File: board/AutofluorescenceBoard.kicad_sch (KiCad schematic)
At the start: 39 parts, among them Q1 Q_PMOS, U1 PAM2863ECR, U2 PAM2863ECR, U3 PAM2863ECR

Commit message: Added LED Footprints and started Layout
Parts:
- D1: footprint (none) -> AF Board:405nm LED
- D3: footprint (none) -> AF Board:365nm LED
- D5: footprint (none) -> AF Board:490nm LED
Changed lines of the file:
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@@
 			)
 		)
-		(property "Footprint" ""
+		(property "Footprint" "AF Board:365nm LED"
 			(at 129.54 31.75 0)
 			(effects
@@
 			)
 		)
-		(property "Footprint" ""
+		(property "Footprint" "AF Board:490nm LED"
 			(at 130.81 139.7 0)
 			(effects
@@
 			)
 		)
-		(property "Footprint" ""
+		(property "Footprint" "AF Board:405nm LED"
 			(at 129.54 87.63 0)
 			(effects

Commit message: Layout Start
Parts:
- D8: footprint ESDALC14-1BF4:ESDALC14-1BF4 -> Resistor_SMD:R_0603_1608Metric
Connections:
- net GND: no longer U2.8 (PGND)
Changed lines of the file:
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@@
 	)
 	(junction
-		(at 107.95 102.87)
-		(diameter 0)
-		(color 0 0 0 0)
-	)
-	(junction
 		(at 60.96 100.33)
 		(diameter 0)
@@
 	)
 	(junction
-		(at 107.95 95.25)
-		(diameter 0)
-		(color 0 0 0 0)
-	)
-	(junction
-		(at 107.95 92.71)
-		(diameter 0)
-		(color 0 0 0 0)
-	)
-	(junction
 		(at 41.91 41.91)
 		(diameter 0)
@@
 	(wire
 		(pts
-			(xy 107.95 92.71) (xy 107.95 95.25)
+			(xy 107.95 92.71) (xy 107.95 97.79)
 		)
 		(stroke
@@
 	(wire
 		(pts
-			(xy 107.95 95.25) (xy 107.95 97.79)
-		)
-		(stroke
-			(width 0)
-			(type default)
-		)
-	)
-	(wire
-		(pts
 			(xy 257.81 83.82) (xy 257.81 86.36)
 		)
@@
 			)
 		)
-		(property "Footprint" "ESDALC14-1BF4:ESDALC14-1BF4"
+		(property "Footprint" "Resistor_SMD:R_0603_1608Metric"
 			(at 256.54 31.75 0)
 			(effects

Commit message: Random Footprint changes
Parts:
- removed D2, D4, D6: D_Schottky, AF Board:Schottky, symbol Device:D_Schottky
- removed D8: D_TVS, Resistor_SMD:R_0603_1608Metric, symbol Device:D_TVS
- removed Q1: Q_PMOS, AF Board:P-MOSFET, symbol Device:Q_PMOS
- removed R5: 10K, AF Board:RES_R0603_ROM-L, symbol Device:R_US
- added CR1, CR2, CR3: SK34A-LTP, SMADO-214AC_MCC, symbol AutofluorescenceBoard:SK34A-LTP
- C1, C2, C3: footprint AF Board:CAP_CL_21_SAM-L -> Capacitor_SMD:C_0805_2012Metric_Pad1.18x1.45mm_HandSolder
- L1, L2, L3: footprint AF Board:Inductor -> AutofluorescenceBoard:SRN6045TA-470M
- R1, R2, R3: value 0.1R -> 0.1; footprint AF Board:TO508P1229X317-3N -> AutofluorescenceBoard:TO508P1229X317-3N
- R4: renamed from R6; footprint AF Board:RES_R0603_ROM-L -> Resistor_SMD:R_0603_1608Metric_Pad0.98x0.95mm_HandSolder
- R5: renamed from R7; footprint AF Board:RES_R0603_ROM-L -> Resistor_SMD:R_0603_1608Metric_Pad0.98x0.95mm_HandSolder
- R6: renamed from R8; footprint AF Board:RES_R0603_ROM-L -> Resistor_SMD:R_0603_1608Metric_Pad0.98x0.95mm_HandSolder
- R7: renamed from R4; footprint AF Board:2.2K Res -> Resistor_SMD:R_0603_1608Metric_Pad0.98x0.95mm_HandSolder
- U1, U2, U3: footprint AF Board:LED_IC -> SOIC_863ECR_DIO; symbol 2025-10-08_01-46-07:PAM2863ECR -> AutofluorescenceBoard:PAM2863ECR
- renumbered D3 to D1, D1 to D2, D5 to D3, D7 to D4
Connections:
- net +12V: now also Conn1.2 (V+Log), CR1.1, CR2.1, CR3.1
- net GND: now also R1.3, R2.3, R3.3; no longer R1.2, R2.2, R3.2
- net at F3.1, TP3.1, U3.2 (ISENSE): now also R3.2; no longer R3.3
- net at L3.2, U3.5 (LX), U3.6 (LX): now also CR3.2
- net at F2.1, TP2.1, U2.2 (ISENSE): now also R2.2; no longer R2.3
- net at L2.2, U2.5 (LX), U2.6 (LX): now also CR2.2
- net at F1.1, TP1.1, U1.2 (ISENSE): now also R1.2; no longer R1.3
- net at L1.2, U1.5 (LX), U1.6 (LX): now also CR1.2
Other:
- note added: "TODO: Reverse Polarity Protection"
- moved on the sheet: Conn1A, Conn1B

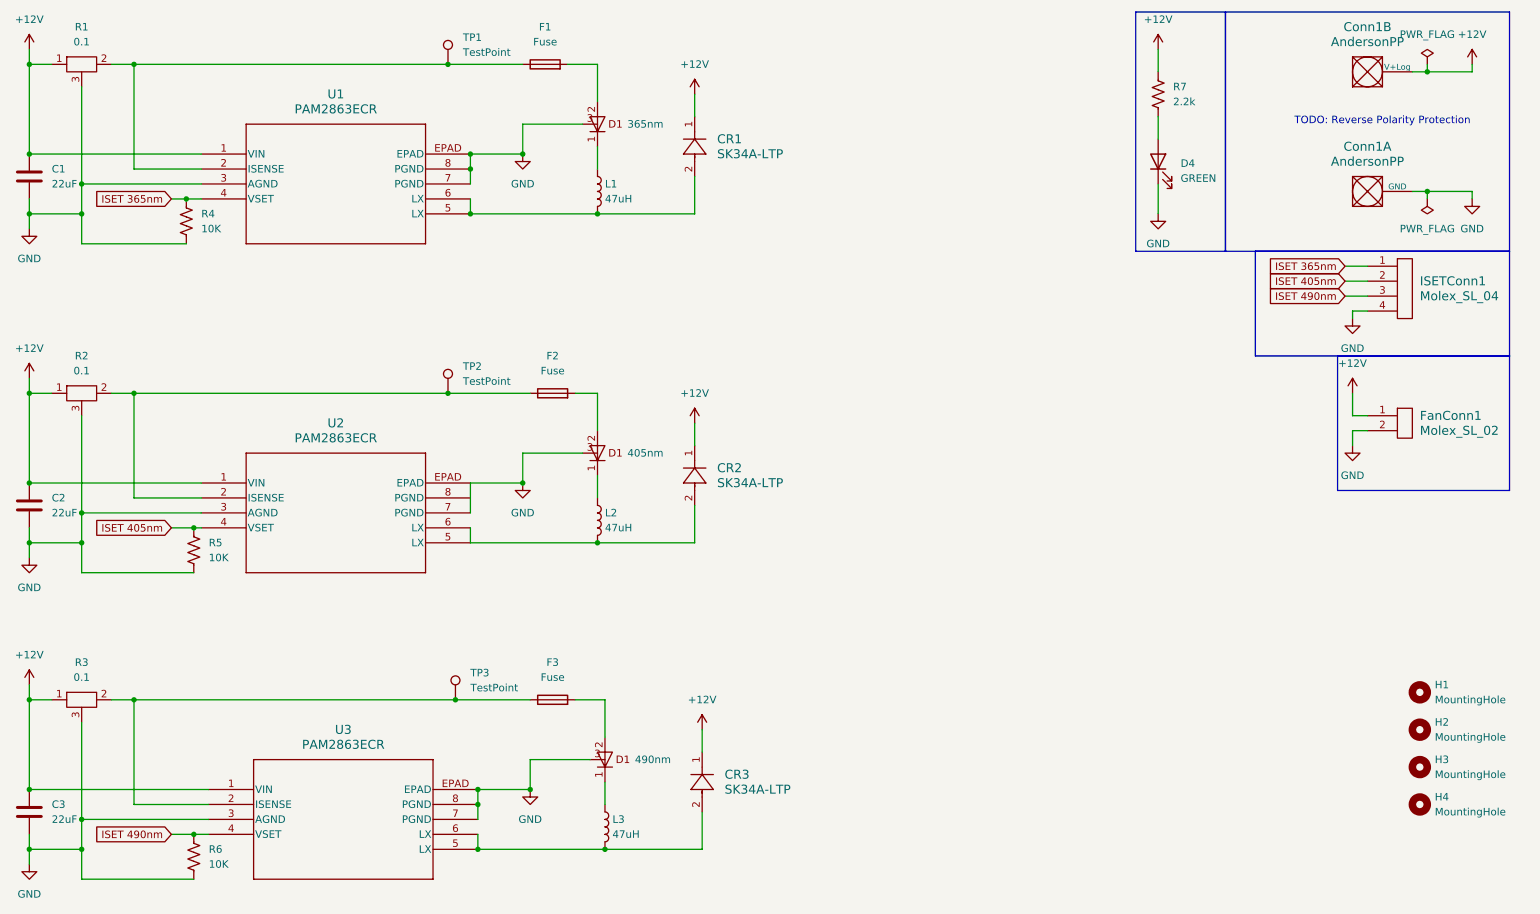
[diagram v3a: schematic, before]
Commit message: Footprints
-Added custom footprints
-added more datasheet links
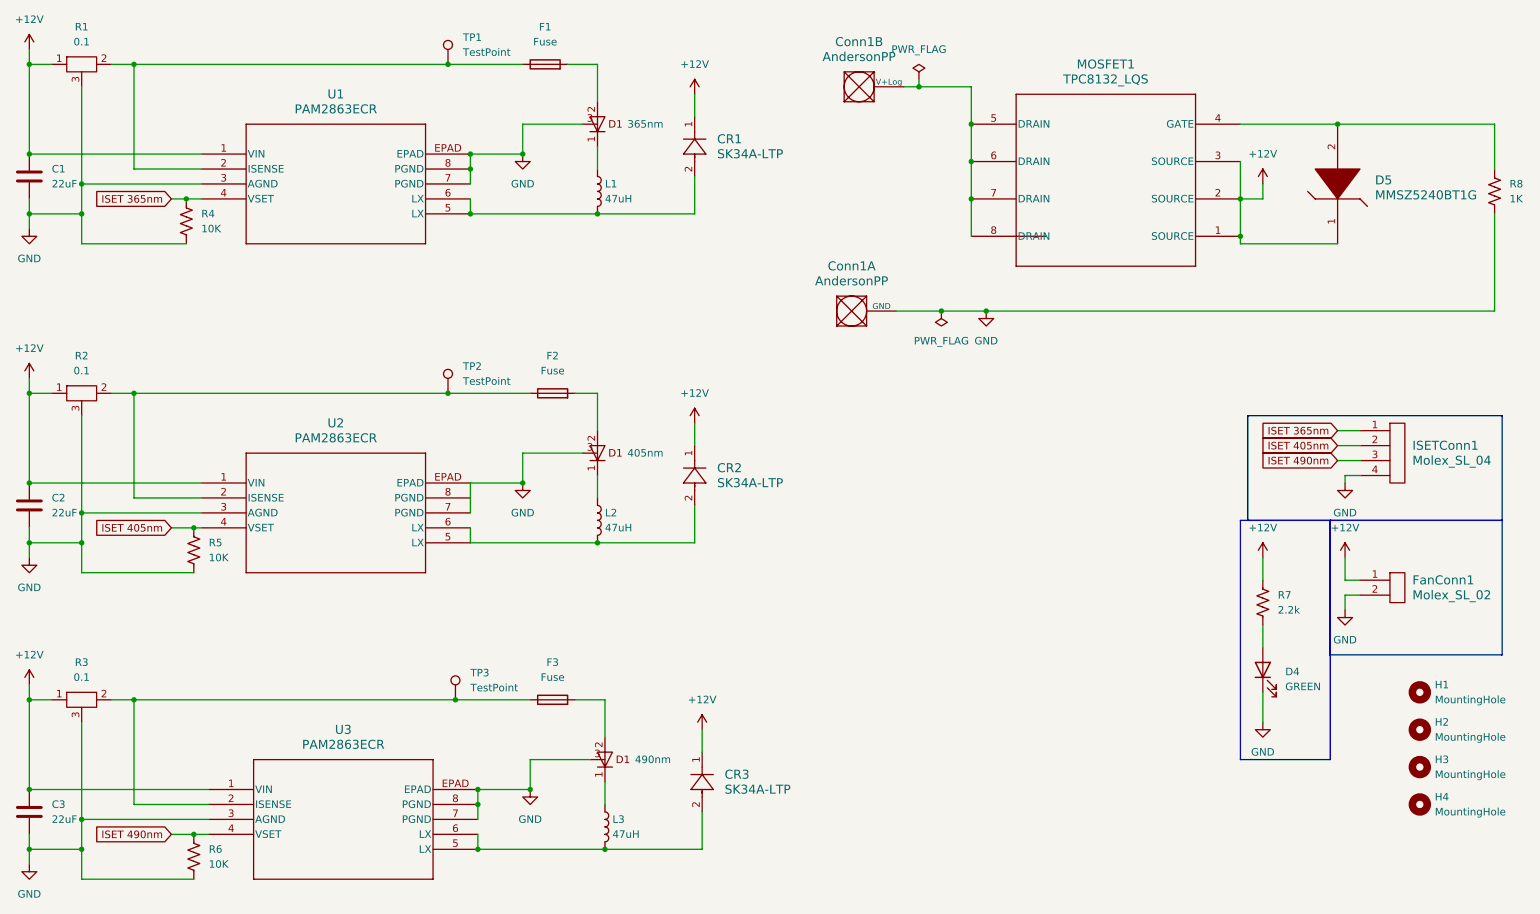
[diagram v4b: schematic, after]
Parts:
- added D5: MMSZ5240BT1G, MRDT_Devices:SOD-123_ONS-L, symbol MRDT_Devices:MMSZ5240BT1G
- added MOSFET1: TPC8132_LQS, MRDT_Devices:SOP-8_TOS-L, symbol MRDT_Devices:TPC8132_LQS
- added R8: 1K, Resistor_SMD:R_0603_1608Metric_Pad0.98x0.95mm_HandSolder, symbol Device:R_US
- D1: footprint AF Board:365nm LED -> AutofluorescenceBoard:365nm
- D2: footprint AF Board:405nm LED -> AutofluorescenceBoard:405nm
- D3: footprint AF Board:490nm LED -> AutofluorescenceBoard:490nm
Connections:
- net +12V: now also D5.1, MOSFET1.1 (SOURCE), MOSFET1.2 (SOURCE), MOSFET1.3 (SOURCE); no longer Conn1.2 (V+Log)
- net GND: now also R8.1
- new net: D5.2, MOSFET1.4 (GATE), R8.2
- new net: Conn1.2 (V+Log), MOSFET1.5 (DRAIN), MOSFET1.6 (DRAIN), MOSFET1.7 (DRAIN), MOSFET1.8 (DRAIN)
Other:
- note removed: "TODO: Reverse Polarity Protection"
- moved on the sheet: Conn1A, Conn1B, D4, FanConn1, ISETConn1, R7

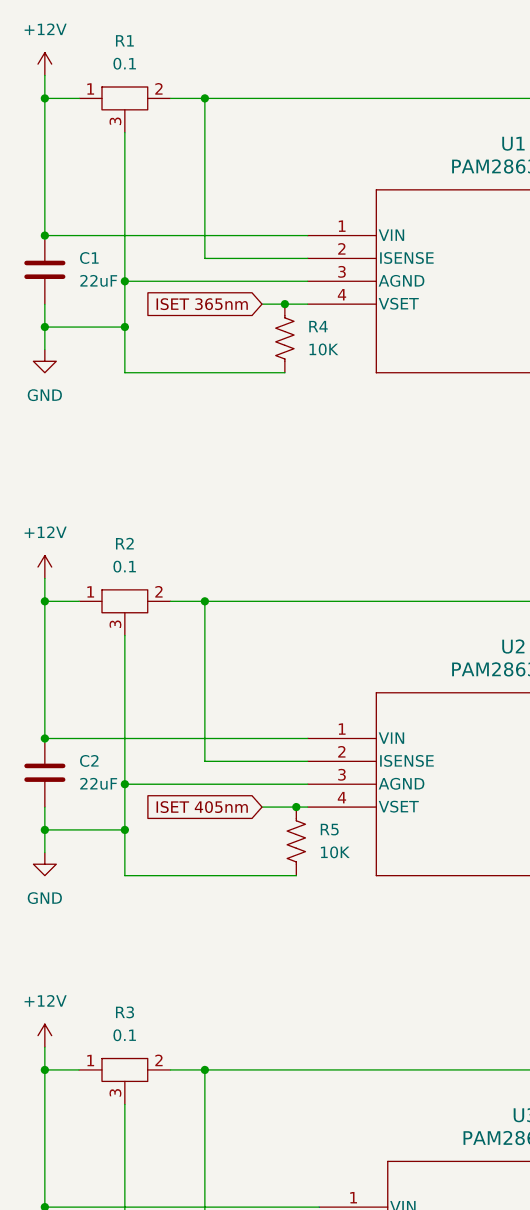
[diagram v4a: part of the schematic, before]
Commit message: Started layout
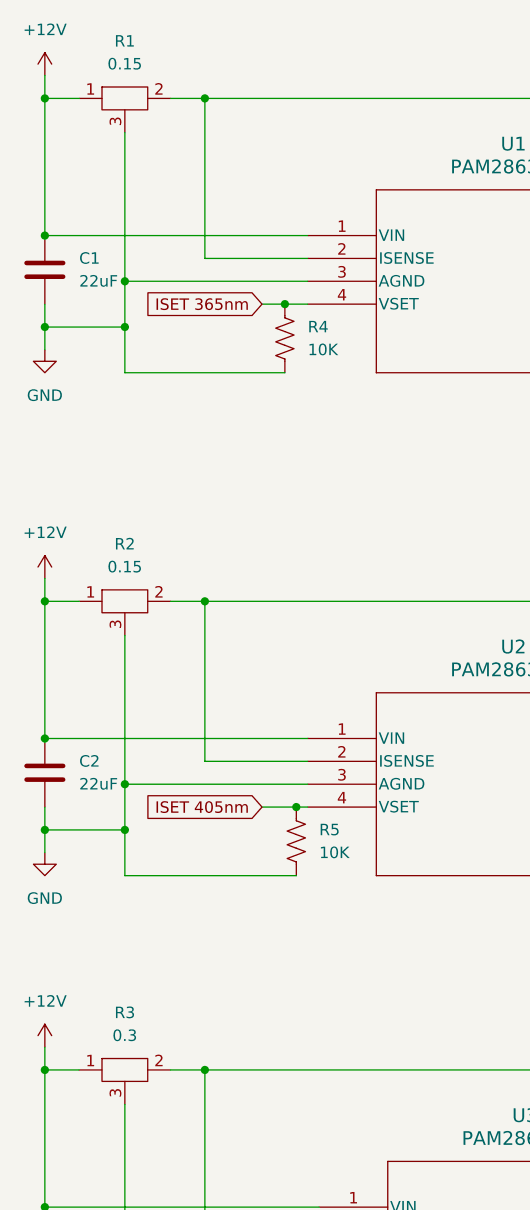
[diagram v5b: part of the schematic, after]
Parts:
- R1, R2: value 0.1 -> 0.15
- R3: value 0.1 -> 0.3

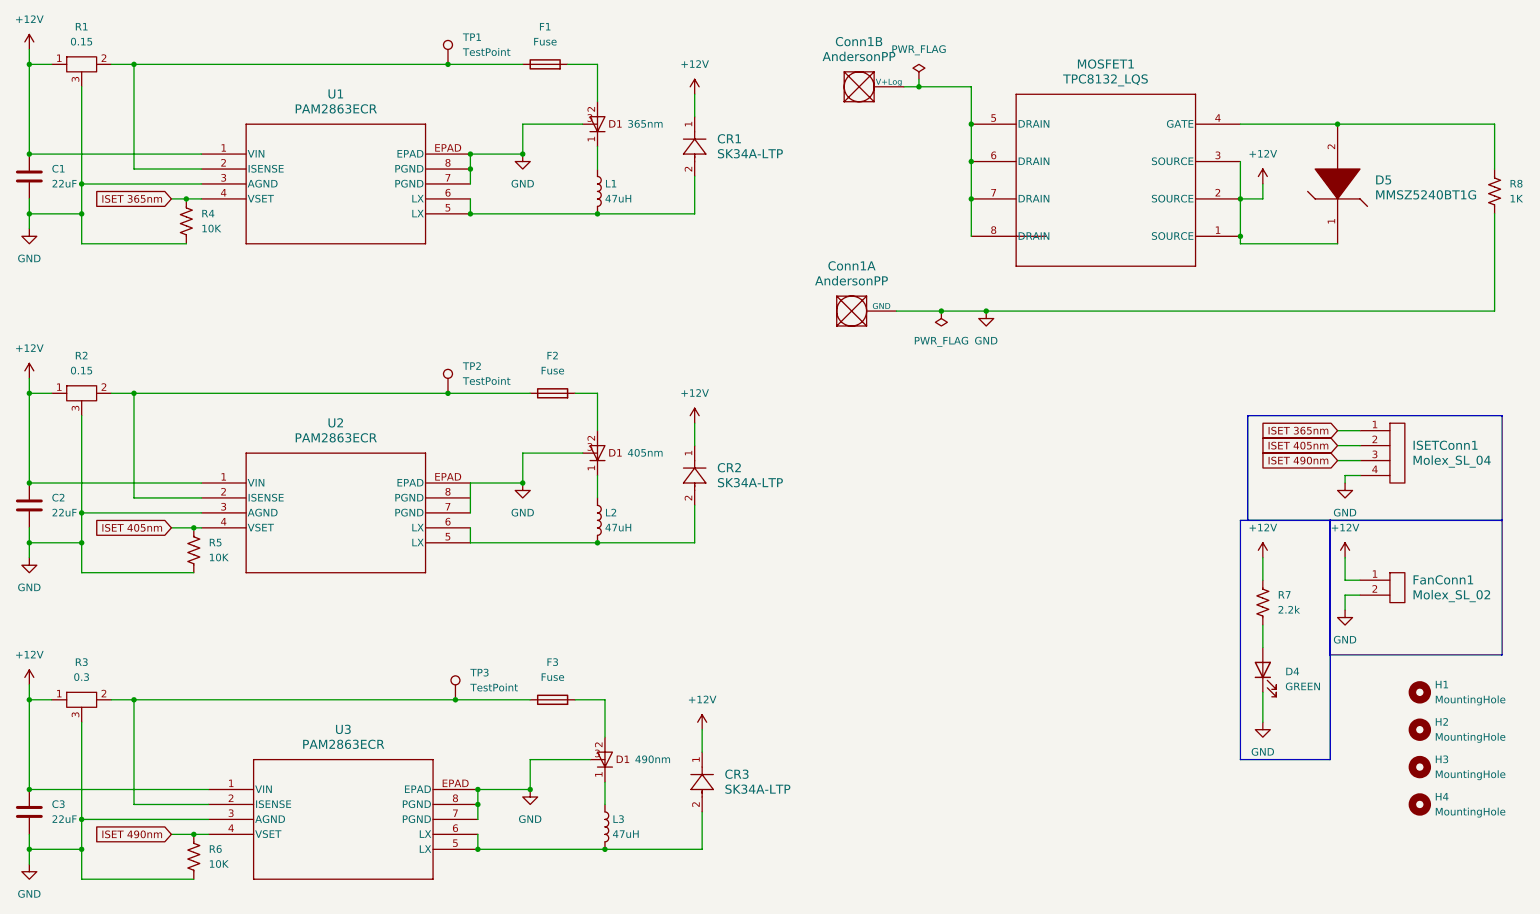
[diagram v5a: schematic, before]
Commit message: First Draft of Layout done
-Traces are proofs of concept. NEED TO BE COMPLETELY REDONE. No current calculation was done and the ground plane is mad T_T
-Board also needs to be actually the size said in CDR presentation. Just didn't want to spend the time perfectly sizing to the value I wanted.
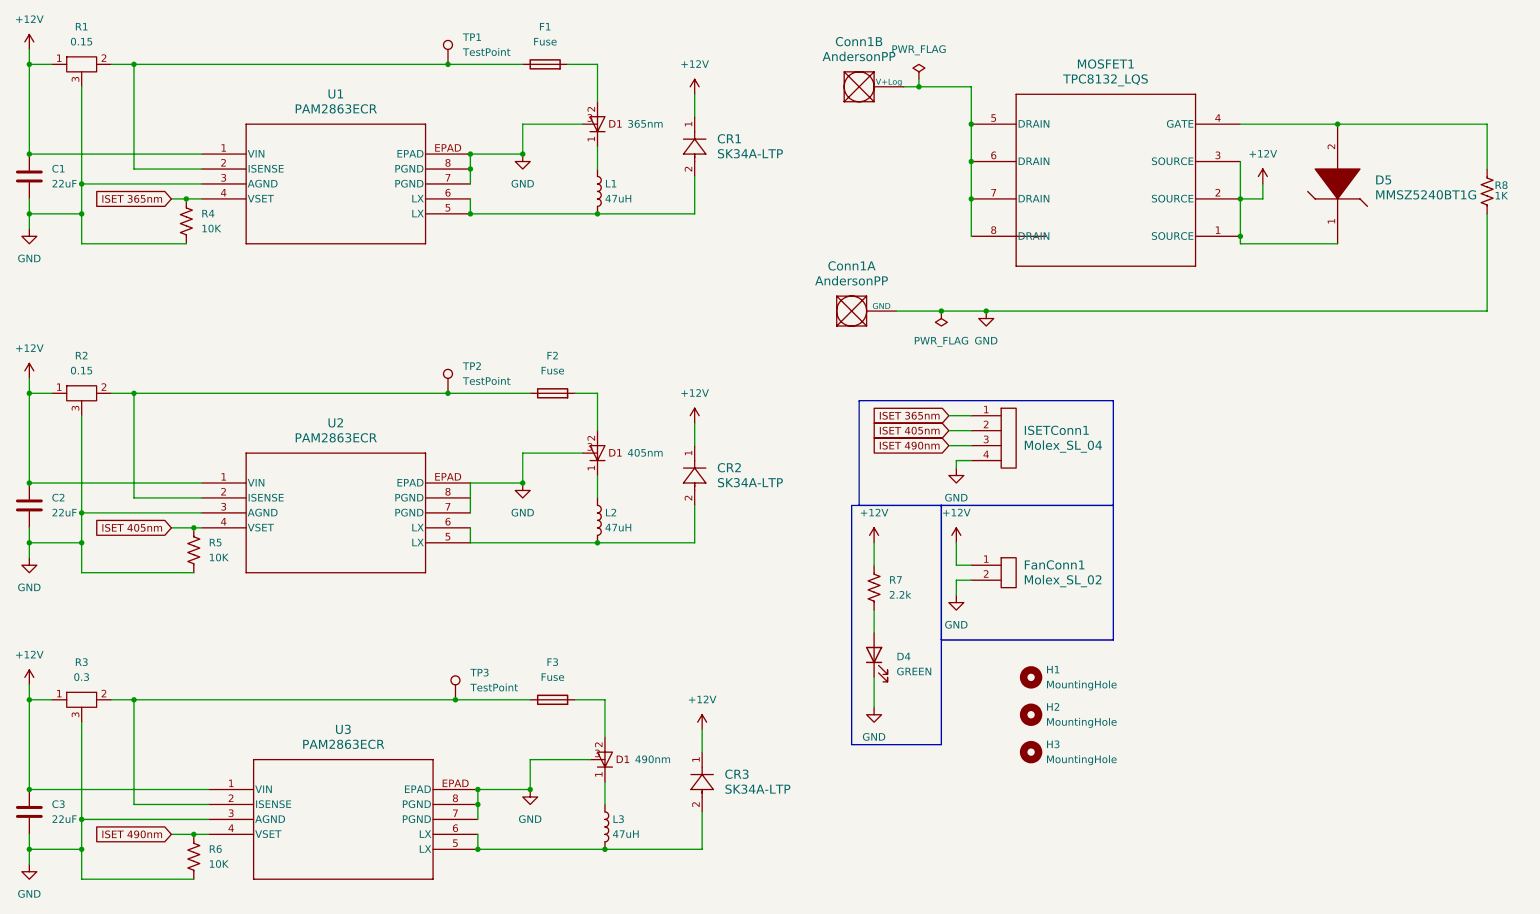
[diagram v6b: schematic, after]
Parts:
- removed H4: MountingHole, MountingHole:MountingHole_3.5mm, symbol Mechanical:MountingHole
- H1, H2, H3: footprint MountingHole:MountingHole_3.5mm -> MRDT_Drill_Holes:6_32_Hole_Corner
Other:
- moved on the sheet: D4, FanConn1, H1, H2, H3, ISETConn1, R7, R8
